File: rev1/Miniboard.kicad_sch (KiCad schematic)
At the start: 23 parts, among them J1 USB_C_Receptacle_USB2.0, SW1 RESET, U2 ATmega32U4-A, Y1 16MHz

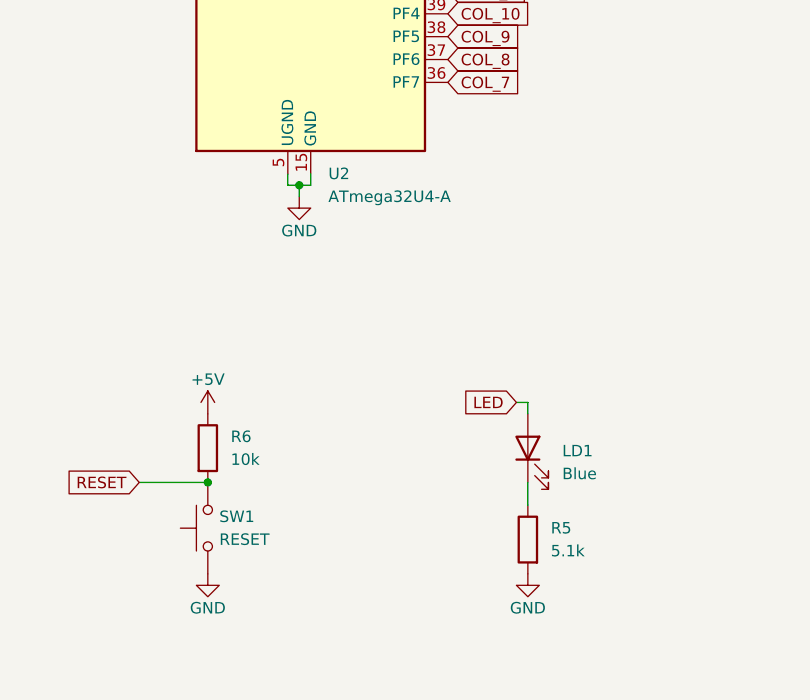
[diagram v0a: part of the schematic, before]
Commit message: Update Rev1.0 silkscreen
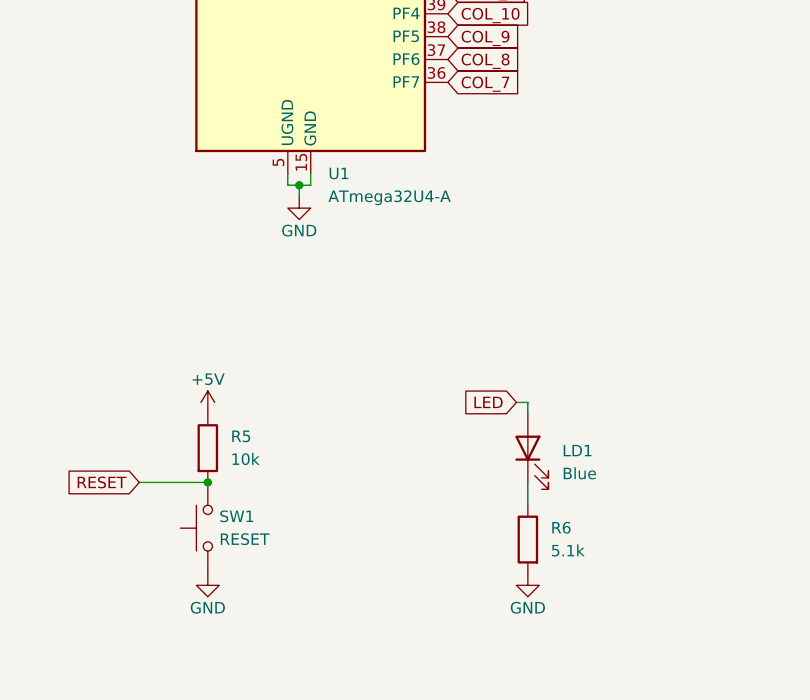
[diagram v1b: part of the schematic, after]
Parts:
- renumbered R6 to R5, R5 to R6, U2 to U1
